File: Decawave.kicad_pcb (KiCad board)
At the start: 4 copper layers, 20 x 40 mm, 46 parts, among them J1 USB_OTG, J2 USART1, J3 PWR, J4 GPIO, SW1 RESET, U1 STM32L443CCTx_u, U2 MCP1700-3302E_SOT23, X1 JTAG-10

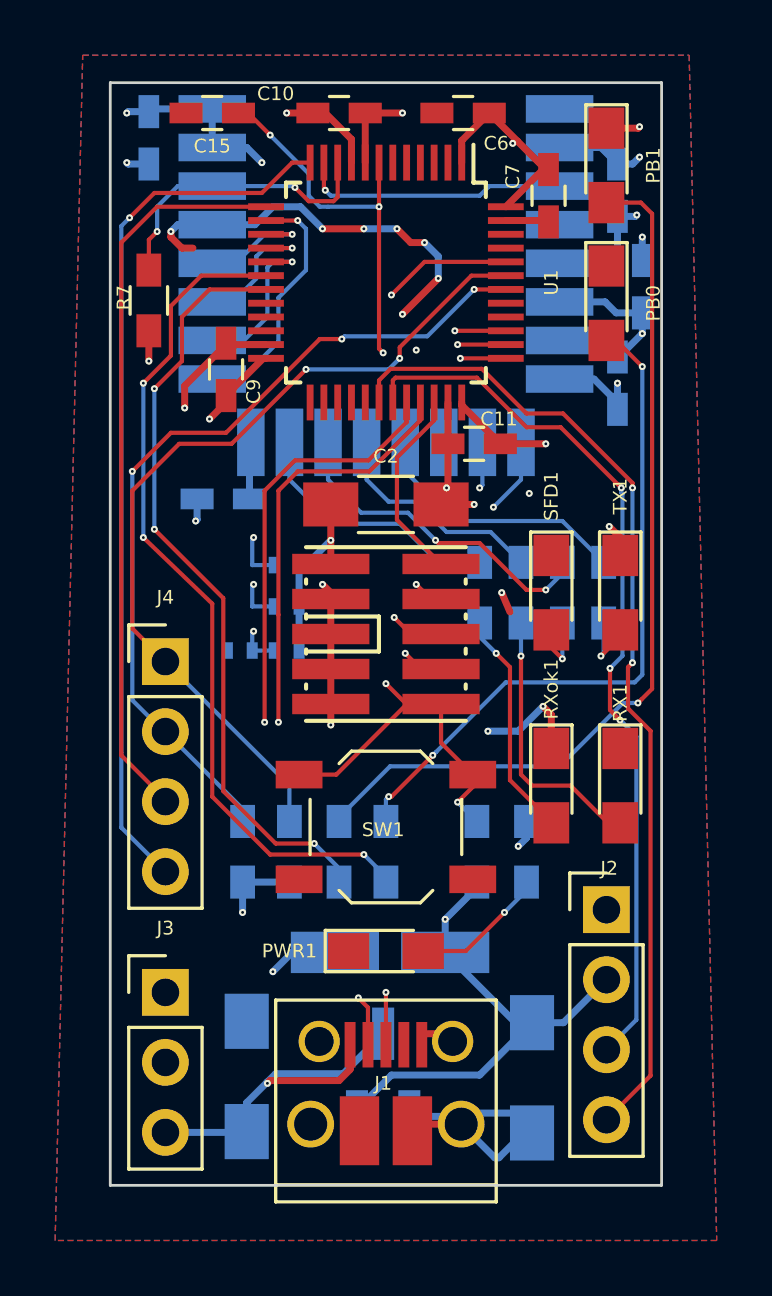
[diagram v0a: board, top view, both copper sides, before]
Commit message: usb footprint, route usb as differential pair
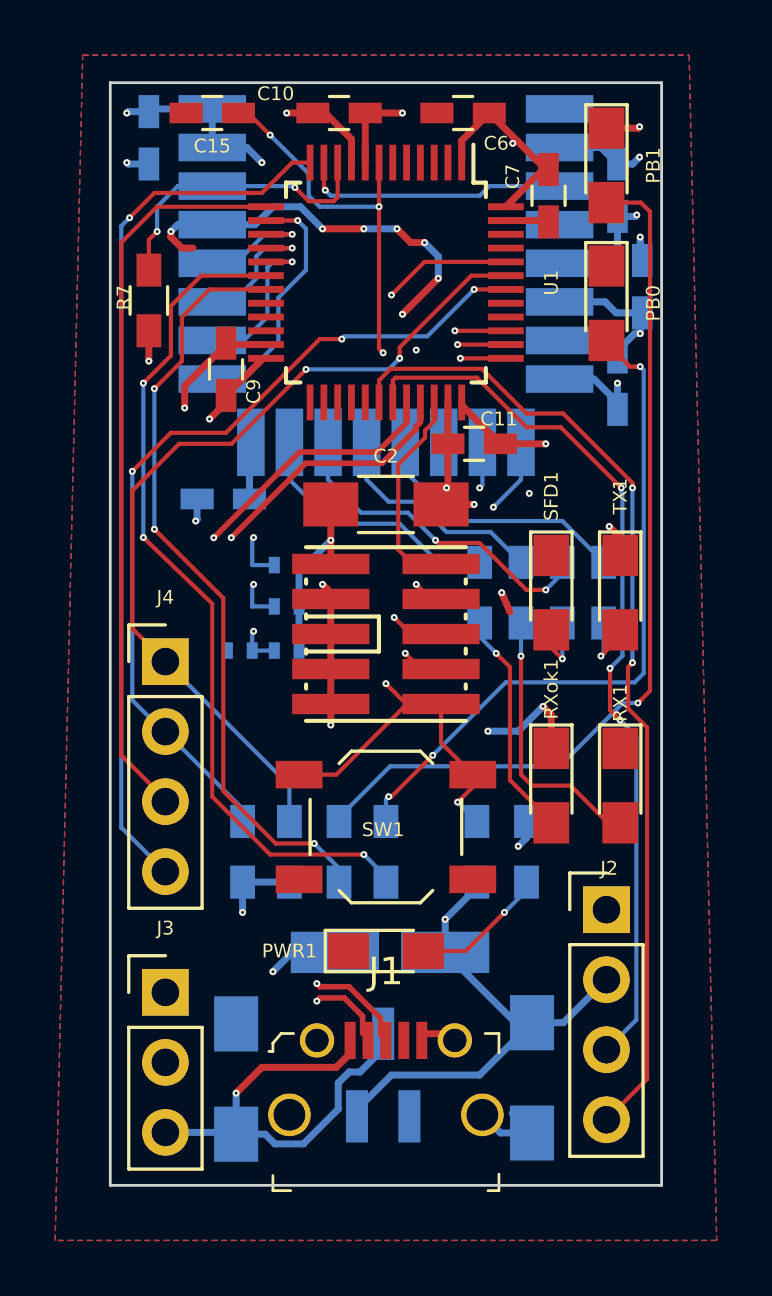
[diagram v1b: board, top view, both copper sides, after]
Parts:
- J1: value USB_OTG -> 10118194-0001LF; footprint Connect:USB_Micro-B_10103594-0001LF -> digikey-footprints:USB_Micro_B_Female_10118194-0001LF
- moved J1 1.66 mm to (70.0, 94.7)
- moved C1 0.39 mm to (64.6, 96.1)
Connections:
- net /PA11USB_DM renamed /USBD_N
- net /PA12USB_DP renamed /USBD_P
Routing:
- net GND: track 81.5 -> 74.8 mm
- net +5V: track 15.7 -> 17.7 mm
- net /USBD_N: track 28.9 -> 30.8 mm
- net /USBD_P: track 29.2 -> 30.7 mm
- net /SWDIO: track 7.08 -> 8.32 mm
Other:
- board text added: "Rev. 2"

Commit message: adding silkscreen for pins
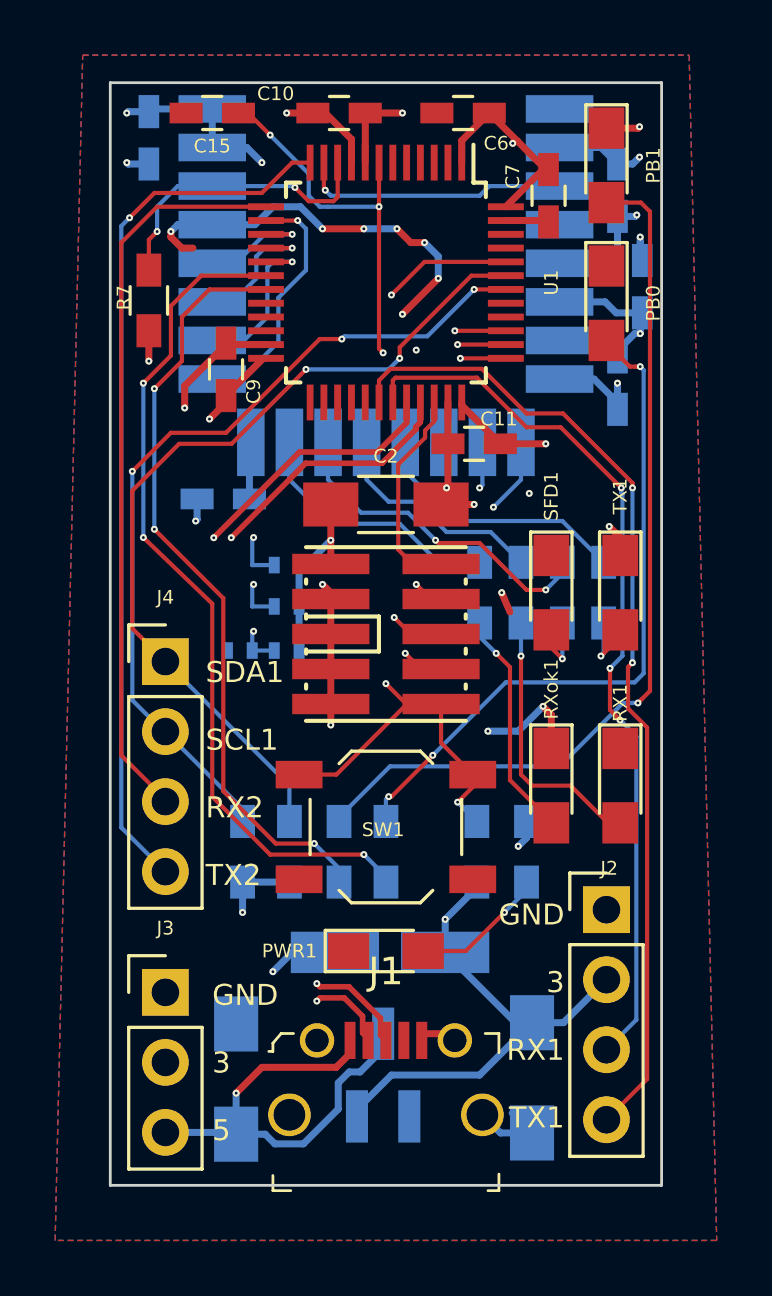
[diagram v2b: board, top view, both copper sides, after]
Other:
- board text added: "GND 3 5"
- board text added: "GND 3 RX1 TX1"
- board text added: "SDA1 SCL1 RX2 TX2"
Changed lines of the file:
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@@
     (area 59.949999 59.949999 80.050001 100.050001)
     (thickness 1.6)
-    (drawings 9)
+    (drawings 12)
     (tracks 575)
     (zones 0)
@@
     )
   )
+  (gr_text "GND\n\n3\n\nRX1\n\nTX1" (at 76.4794 93.8657) (layer F.SilkS)
+    (effects (font (size 0.762 0.762) (thickness 0.127)) (justify right))
+  )
+  (gr_text "GND\n\n3\n\n5" (at 63.69812 95.5548) (layer F.SilkS)
+    (effects (font (size 0.762 0.762) (thickness 0.127)) (justify left))
+  )
+  (gr_text "SDA1\n\nSCL1\n\nRX2\n\nTX2\n" (at 63.45682 85.06968) (layer F.SilkS)
+    (effects (font (size 0.762 0.762) (thickness 0.127)) (justify left))
+  )
   (gr_text "Rev. 2" (at 61.40196 66.54038 270) (layer B.SilkS)

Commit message: adding more space for usb connector
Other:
- outline, holes or cut-outs redrawn
- board text added: "Rev. 2.1"
- board text removed: "Rev. 2"
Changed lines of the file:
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@@
     (area 59.949999 59.949999 80.050001 100.050001)
     (thickness 1.6)
-    (drawings 12)
+    (drawings 16)
     (tracks 575)
     (zones 0)
@@
     (2 In2.Cu mixed hide)
     (31 B.Cu signal hide)
-    (32 B.Adhes user)
-    (33 F.Adhes user)
-    (34 B.Paste user)
-    (35 F.Paste user)
+    (32 B.Adhes user hide)
+    (33 F.Adhes user hide)
+    (34 B.Paste user hide)
+    (35 F.Paste user hide)
     (36 B.SilkS user)
-    (37 F.SilkS user)
-    (38 B.Mask user)
-    (39 F.Mask user)
-    (40 Dwgs.User user)
-    (41 Cmts.User user)
-    (42 Eco1.User user)
-    (43 Eco2.User user)
-    (44 Edge.Cuts user)
-    (45 Margin user)
-    (46 B.CrtYd user)
-    (47 F.CrtYd user)
-    (48 B.Fab user)
-    (49 F.Fab user)
+    (37 F.SilkS user hide)
+    (38 B.Mask user hide)
+    (39 F.Mask user hide)
+    (40 Dwgs.User user hide)
+    (41 Cmts.User user hide)
+    (42 Eco1.User user hide)
+    (43 Eco2.User user hide)
+    (44 Edge.Cuts user hide)
+    (45 Margin user hide)
+    (46 B.CrtYd user hide)
+    (47 F.CrtYd user hide)
+    (48 B.Fab user hide)
+    (49 F.Fab user hide)
   )
   (setup
@@
     )
   )
+  (gr_line (start 74 100) (end 80 100) (layer Edge.Cuts) (width 0.1))
+  (gr_line (start 74 99) (end 74 100) (layer Edge.Cuts) (width 0.1))
+  (gr_line (start 66 99) (end 74 99) (layer Edge.Cuts) (width 0.1))
+  (gr_line (start 66 100) (end 66 99) (layer Edge.Cuts) (width 0.1))
+  (gr_line (start 60 100) (end 66 100) (layer Edge.Cuts) (width 0.1))
   (gr_text "GND\n\n3\n\nRX1\n\nTX1" (at 76.4794 93.8657) (layer F.SilkS)
     (effects (font (size 0.762 0.762) (thickness 0.127)) (justify right))
@@
     (effects (font (size 0.762 0.762) (thickness 0.127)) (justify left))
   )
-  (gr_text "Rev. 2" (at 61.40196 66.54038 270) (layer B.SilkS)
+  (gr_text "Rev. 2.1" (at 61.40196 66.54038 270) (layer B.SilkS)
     (effects (font (size 0.762 0.762) (thickness 0.127)) (justify mirror))
   )
@@
   )
   (gr_line (start 60 100) (end 60 60) (angle 90) (layer Edge.Cuts) (width 0.1))
-  (gr_line (start 80 100) (end 60 100) (angle 90) (layer Edge.Cuts) (width 0.1))
   (gr_line (start 80 60) (end 80 100) (angle 90) (layer Edge.Cuts) (width 0.1))
   (gr_line (start 60 60) (end 80 60) (angle 90) (layer Edge.Cuts) (width 0.1))
